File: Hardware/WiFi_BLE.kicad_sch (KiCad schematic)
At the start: 8 parts, among them Y1 2016-4P 40MHz

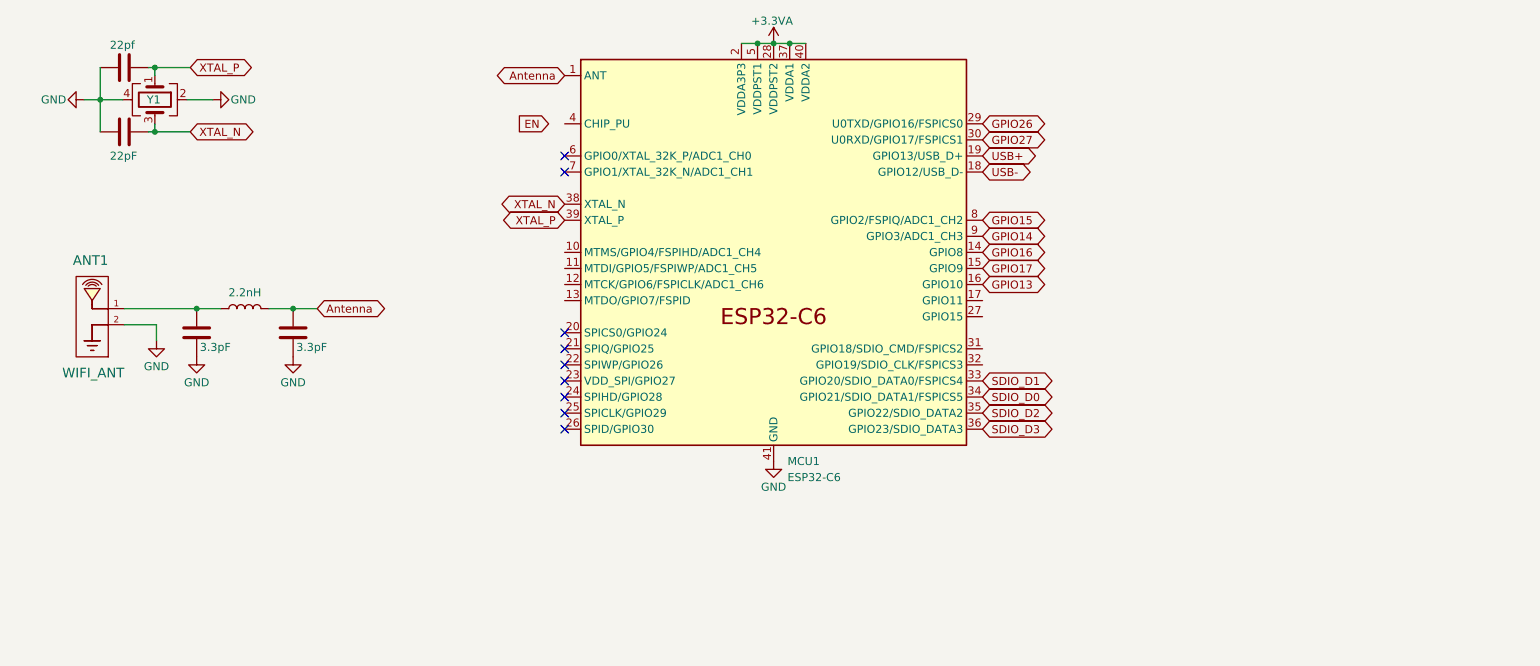
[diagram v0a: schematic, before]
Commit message: 11/19 update
add new header for jtag and fixed a couple of small things
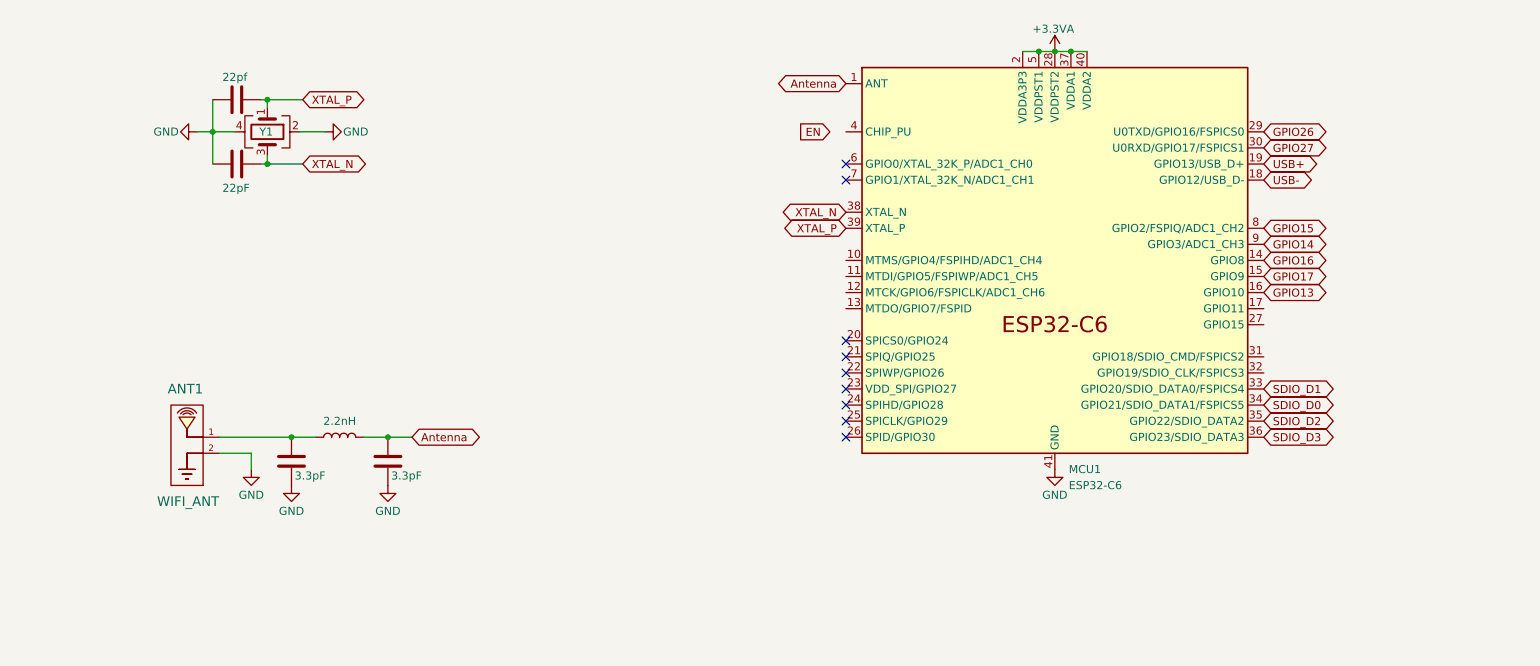
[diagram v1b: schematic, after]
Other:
- moved on the sheet: ANT1, MCU1, Y1

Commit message: 11/21 update
finished annotating the schematic and add pictures and output the pdf
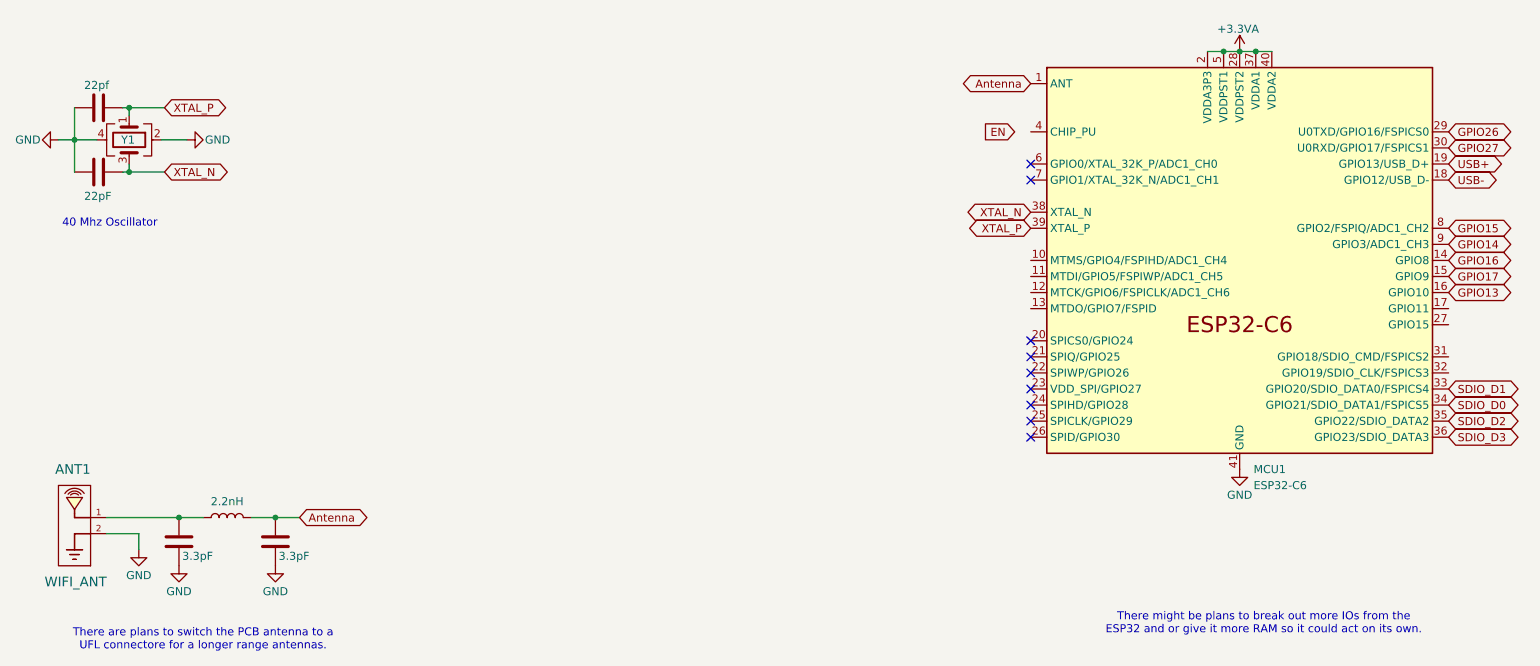
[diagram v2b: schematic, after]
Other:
- note added: "40 Mhz Oscillator"
- note added: "There are plans to switch the PCB antenna to a UFL connectore for a longer range antennas."
- note added: "There might be plans to break out more IOs from the ESP32 and or give it more RAM so it could act on its own."
- moved on the sheet: ANT1, MCU1, Y1
